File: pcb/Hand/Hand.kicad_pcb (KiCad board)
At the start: 4 copper layers, 76.2 x 50.8 mm, 39 parts, among them J10 Conn_01x03_HALL_7, J11 Conn_01x03_HALL_8, J12 Conn_01x03_HALL_9, J13 Conn_01x03_HALL_10, J14 Conn_01x03_HALL_11, J15 Conn_01x03_HALL_12, J16 Conn_01x03_HALL_13, J17 Conn_01x03_HALL_14, J18 Conn_01x03_HALL_15, J19 Conn_01x05_HAPTIC_1, J2 Conn_01x03_HALL_0, J20 Conn_01x05_HAPTIC_2, J21 Conn_01x05_HAPTIC_3, J22 Conn_01x05_HAPTIC_4, J23 Conn_01x03_FEEDBACK_0, J24 Conn_01x03_FEEDBACK_1, J25 Conn_01x03_FEEDBACK_2, J26 Conn_01x03_FEEDBACK_3, J27 Conn_01x03_FEEDBACK_4, J28 Conn_01x03_SPOOLPOT_1, J29 Conn_01x03_SPOOLPOT_2, J3 Conn_01x05_HAPTIC_0, J30 Conn_01x03_SPOOLPOT_3, J31 Conn_01x03_SPOOLPOT_0, J32 Conn_01x03_SPOOLPOT_4, J33 Conn_01x12_Ribbon_Top, J34 Conn_01x12_Ribbon_Bottom, J35 Conn_01x02_Feedback_Power, J4 Conn_01x03_HALL_1, J5 Conn_01x03_HALL_2, J6 Conn_01x03_HALL_3, J7 Conn_01x03_HALL_4, J8 Conn_01x03_HALL_5, J9 Conn_01x03_HALL_6, U1 CD74HC4067M96, U2 4754, U3 TCA9548A

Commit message: completed tentative part layout
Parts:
- C1, J10, J11, J12, J13, J14, J15, J16, J17, J18, J19, J2, J20, J21, J22, J3, J4, J5, J6, J7, J8, J9, U1, U3: moved to B.Cu
- moved J6 168.6 mm to (17.9, 30.7), turned to 90 degrees
- moved J12 158.8 mm to (33.8, 40.6)
- moved J5 155.9 mm to (18.0, 23.6), turned to 90 degrees
- moved J11 151.3 mm to (33.8, 33.0)
- moved J13 147.6 mm to (47.2, 25.6)
- moved J10 146.4 mm to (33.8, 25.6), turned to 0 degrees
- moved J4 142.7 mm to (23.9, 18.0), turned to 0 degrees
- moved J2 142.7 mm to (16.8, 18.0), turned to 0 degrees
- moved J18 117.7 mm to (83.8, 18.0)
- moved J14 109.2 mm to (47.2, 33.2)
- moved J16 109.1 mm to (54.9, 33.2)
- moved J15 108.6 mm to (54.9, 25.6)
- moved J3 101.6 mm to (32.0, 14.1)
- moved J17 101.3 mm to (76.7, 18.0)
- moved U1 99.6 mm to (51.3, 44.2)
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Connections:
- J23 pad 2: GND -> 6V0_GND
- J24 pad 2: GND -> 6V0_GND
- J25 pad 2: GND -> 6V0_GND
- J26 pad 2: GND -> 6V0_GND
- J27 pad 2: GND -> 6V0_GND

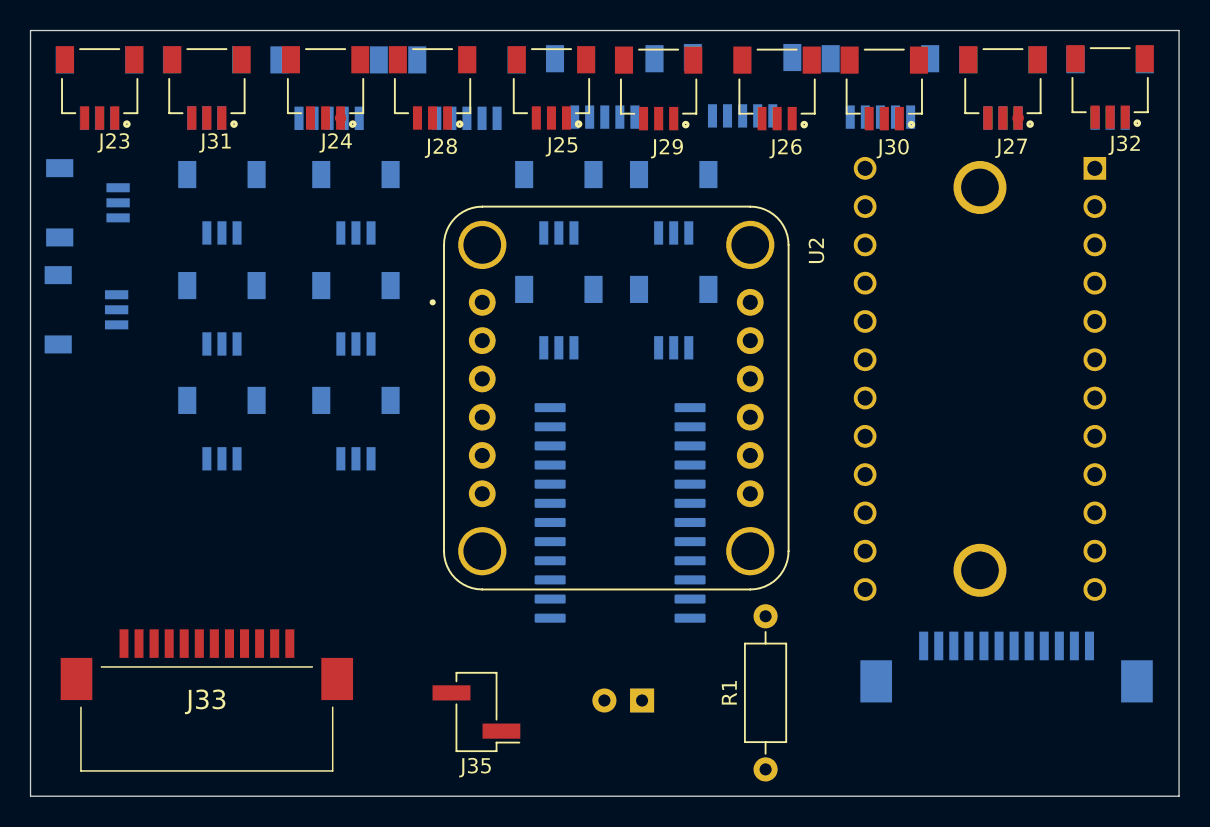
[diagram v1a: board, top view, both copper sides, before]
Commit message: updated and routed hand pcb
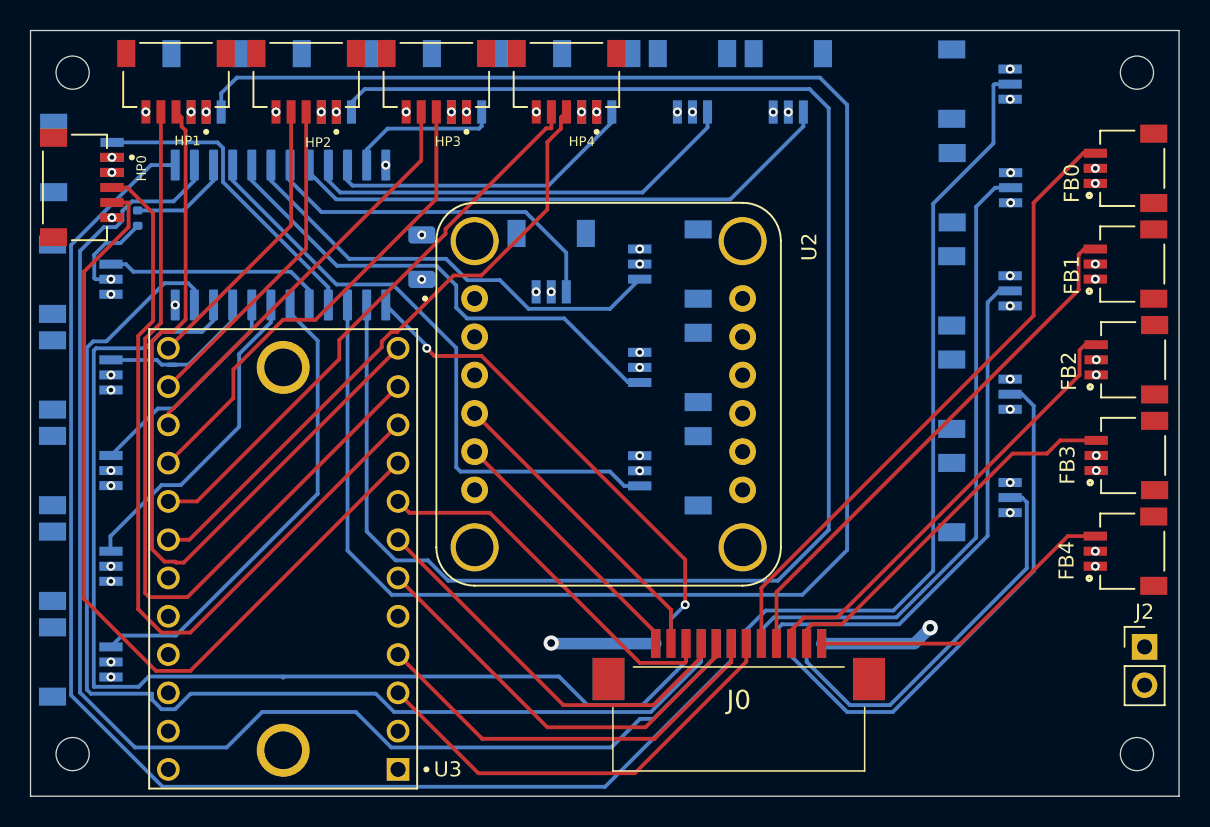
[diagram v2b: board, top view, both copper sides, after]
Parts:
- added REF**: MountingHole_2.2mm_M2, MountingHole:MountingHole_2.2mm_M2, F.Cu at (85.6, 60.2)
- added REF**: MountingHole_2.2mm_M2, MountingHole:MountingHole_2.2mm_M2, F.Cu at (15.0, 15.0)
- added REF**: MountingHole_2.2mm_M2, MountingHole:MountingHole_2.2mm_M2, F.Cu at (15.0, 60.2)
- added REF**: MountingHole_2.2mm_M2, MountingHole:MountingHole_2.2mm_M2, F.Cu at (85.6, 15.0)
- C1: footprint Capacitor_THT:CP_Radial_D5.0mm_P2.50mm -> Capacitor_SMD:C_1206_3216Metric
- HP0: renamed from J3; moved to F.Cu
- HP1: renamed from J19; moved to F.Cu
- HP2: renamed from J20; moved to F.Cu
- HP3: renamed from J21; moved to F.Cu
- HP4: renamed from J22; moved to F.Cu
- J2: renamed from J35; footprint Connector_PinHeader_2.54mm:PinHeader_1x02_P2.54mm_Vertical_SMD_Pin1Left -> Connector_PinHeader_2.54mm:PinHeader_1x02_P2.54mm_Vertical
- R1: footprint Resistor_THT:R_Axial_DIN0207_L6.3mm_D2.5mm_P10.16mm_Horizontal -> Resistor_SMD:R_0402_1005Metric; moved to B.Cu
- SP0: renamed from J31; moved to B.Cu
- SP1: renamed from J28; moved to B.Cu
- SP2: renamed from J29; moved to B.Cu
- SP3: renamed from J30; moved to B.Cu
- SP4: renamed from J32; moved to B.Cu
- U3: moved to F.Cu
- moved FB0 66.1 mm to (82.8, 21.3), turned to 90 degrees
- moved R1 55.4 mm to (19.3, 24.6)
- moved SP0 53.3 mm to (77.2, 15.7), turned to 90 degrees
- moved FB1 52.0 mm to (82.8, 27.7), turned to 90 degrees
- moved U3 47.7 mm to (29.0, 47.2)
- moved J2 44.5 mm to (86.1, 53.1), turned to 0 degrees
- moved FB2 39.5 mm to (82.9, 34.0), turned to 90 degrees
- moved H4F2 39.0 mm to (52.6, 41.4), turned to -90 degrees
- moved SP1 38.6 mm to (77.2, 22.6), turned to 90 degrees
- moved J0 35.3 mm to (59.2, 53.8)
- moved C1 32.8 mm to (38.2, 27.2), turned to -90 degrees
- moved FB3 30.8 mm to (82.9, 40.4), turned to 90 degrees
- moved FB4 29.4 mm to (82.8, 46.7), turned to 90 degrees
- moved H4F1 29.2 mm to (52.6, 34.5), turned to -90 degrees
- moved U1 29.1 mm to (28.8, 25.8), turned to 90 degrees
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- renumbered J23 to FB0, J24 to FB1, J25 to FB2, J26 to FB3, J27 to FB4, J7 to H1F0, J8 to H1F1, J9 to H1F2, J10 to H2F0, J11 to H2F1, J12 to H2F2, J13 to H3F0, J14 to H3F1, J15 to H3F2, J16 to H4F0, J17 to H4F1, J18 to H4F2, J2 to HTH0, J4 to HTH1, J5 to HTH2, J6 to HTH3, J33 to J0, J34 to J1
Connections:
- J0 pad 1: SPOOLPOT_ADC0 -> IMU_SDA
- J0 pad 10: FEEDBACK_D4 -> FEEDBACK_D2
- J0 pad 11: IMU_SCL -> FEEDBACK_D3
- J0 pad 12: IMU_SDA -> FEEDBACK_D4
- J0 pad 2: SPOOLPOT_ADC1 -> IMU_SCL
- J0 pad 3: SPOOLPOT_ADC2 -> HAPTIC_S2
- J0 pad 4: SPOOLPOT_ADC3 -> HAPTIC_S1
- J0 pad 5: SPOOLPOT_ADC4 -> HAPTIC_S0
- J0 pad 6: FEEDBACK_D0 -> HAPTIC_SCL
- J0 pad 7: FEEDBACK_D1 -> HAPTIC_SDA
- J0 pad 8: FEEDBACK_D2 -> FEEDBACK_D0
- J0 pad 9: FEEDBACK_D3 -> FEEDBACK_D1
- J1 pad 10: HAPTIC_SCL -> HALL_S0
- J1 pad 11: HAPTIC_SDA -> HALL_ADC
- J1 pad 2: HALL_ADC -> SPOOLPOT_ADC4
- J1 pad 3: HALL_S0 -> SPOOLPOT_ADC3
- J1 pad 4: HALL_S1 -> SPOOLPOT_ADC2
- J1 pad 5: HALL_S2 -> SPOOLPOT_ADC1
- J1 pad 6: HALL_S3 -> SPOOLPOT_ADC0
- J1 pad 7: HAPTIC_S0 -> HALL_S3
- J1 pad 8: HAPTIC_S1 -> HALL_S2
- J1 pad 9: HAPTIC_S2 -> HALL_S1
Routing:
- net HALL_6: track 0.00 -> 125.4 mm
- net HALL_7: track 0.00 -> 109.6 mm
- net HALL_S3: track 0.00 -> 89.9 mm
- net HALL_S2: track 0.00 -> 89.2 mm
- net HALL_S1: track 0.00 -> 77.8 mm
- net HALL_S0: track 0.00 -> 74.9 mm
- net HAPTIC_SDA_0: track 0.00 -> 57.1 mm
- net HAPTIC_SDA_1: track 0.00 -> 55.0 mm
- net HAPTIC_SCL_0: track 0.00 -> 53.7 mm
- net HAPTIC_SCL_1: track 0.00 -> 53.2 mm
- net SPOOLPOT_ADC0: track 0.00 -> 49.9 mm
- net SPOOLPOT_ADC1: track 0.00 -> 42.5 mm
- net FEEDBACK_D0: track 0.00 -> 42.2 mm
- net HAPTIC_SCL_4: track 0.00 -> 41.4 mm
- net HALL_15: track 0.00 -> 41.1 mm
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- added copper zone on In1.Cu, net 6V0
- added copper zone on In2.Cu, net 6V0_GND

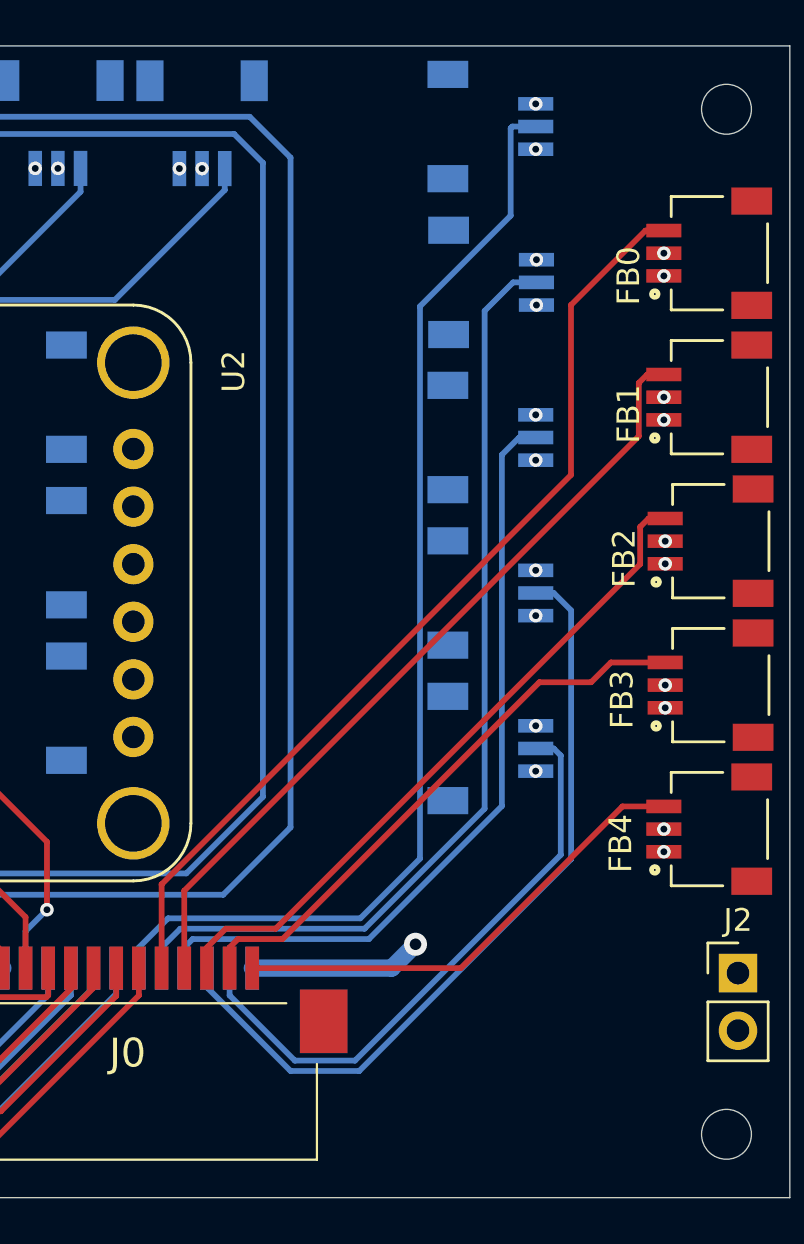
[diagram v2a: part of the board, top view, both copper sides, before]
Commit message: revised hand and made pass at routing forearm pcb
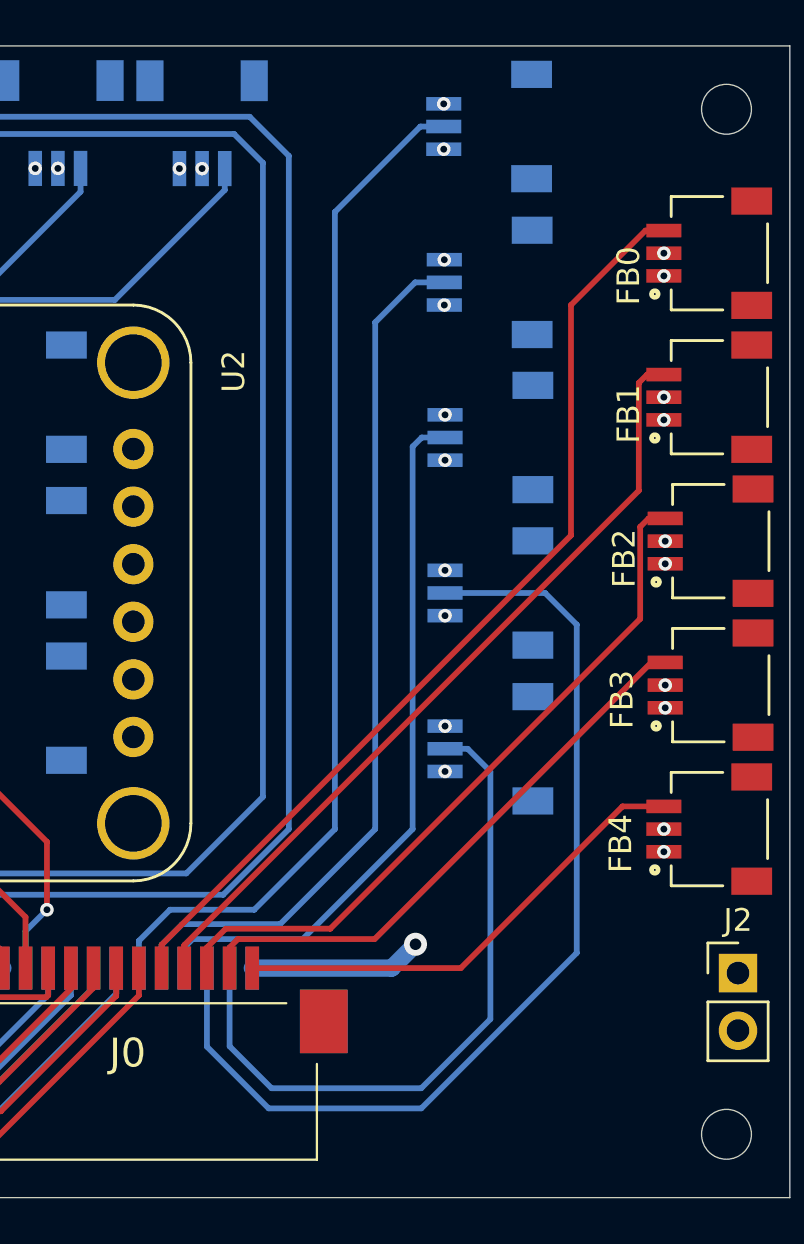
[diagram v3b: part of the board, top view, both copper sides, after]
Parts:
- moved SP1 4.06 mm to (73.2, 22.6), turned to -90 degrees
- moved SP0 4.06 mm to (73.1, 15.7), turned to -90 degrees
- moved SP4 4.00 mm to (73.2, 43.2), turned to -90 degrees
- moved SP2 4.00 mm to (73.2, 29.5), turned to -90 degrees
- moved SP3 4.00 mm to (73.2, 36.3), turned to -90 degrees
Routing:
- net SPOOLPOT_ADC3: track 35.2 -> 44.6 mm
- net SPOOLPOT_ADC0: track 49.9 -> 45.5 mm
- net SPOOLPOT_ADC4: track 26.4 -> 30.3 mm
- net SPOOLPOT_ADC1: track 42.5 -> 38.7 mm
- net SPOOLPOT_ADC2: track 34.8 -> 31.6 mm
- net FEEDBACK_D2: track 29.9 -> 31.3 mm
